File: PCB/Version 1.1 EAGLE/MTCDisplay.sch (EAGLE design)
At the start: 38 parts, among them IC1 74HC14N, J1 POWER_JACKPTH, U1 ATMEGA328P_PDIP, U2 57PC5FSWITCHCRAFT, U3 57PC5FSWITCHCRAFT, U4 57PC5FSWITCHCRAFT, U5 57PC5FSWITCHCRAFT, U6 MAX7219DIP, Y1 16MHz

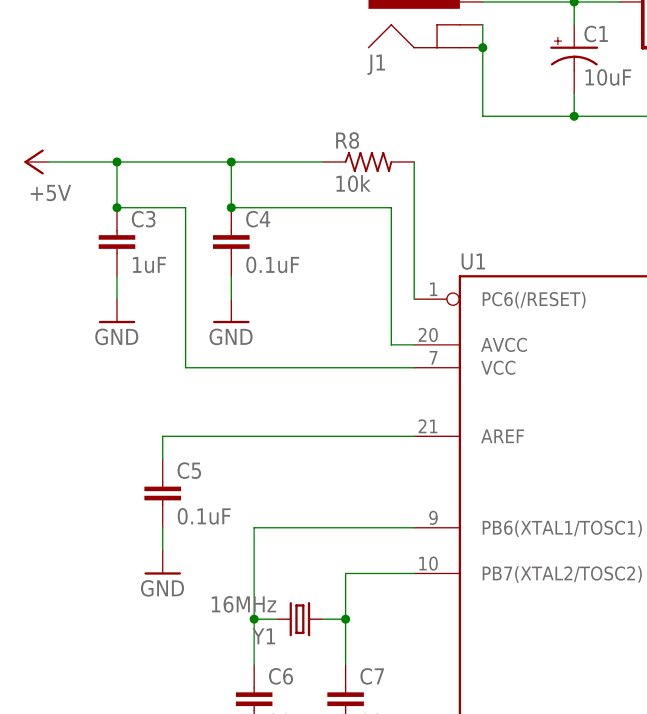
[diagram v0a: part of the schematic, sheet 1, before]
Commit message: update v1.1 schematics (replace 0.1uF cap package, add part names)
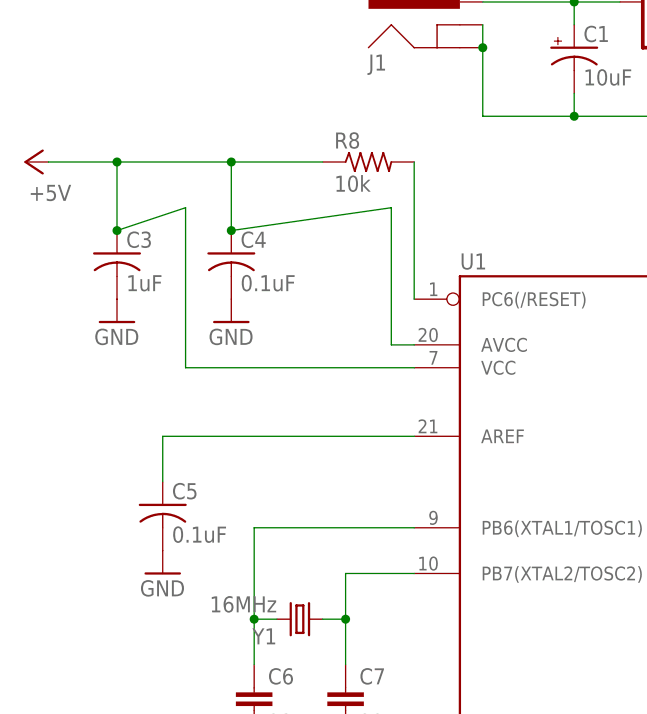
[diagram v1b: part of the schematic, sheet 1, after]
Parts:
- C10, C3, C4, C5, C8, C9: device SparkFun-Capacitors:0.1UF-50V-20%(PTH)KIT-EZ -> rcl:C-US025-025X050
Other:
- moved on the sheet: C10, C3, C4, C5, C8, C9

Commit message: Remove MIDI OUT, replace all TH capacitor with SMD
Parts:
- removed S1: RX-TX, SparkFun-Electromechanical:SWITCH-SPDTPTH
- C1, C11: value 10uF -> 10u; device resistor:CPOL-USE2-5 -> rcl:C-USC0805K
- C10, C4, C5, C8, C9: value 0.1uF -> 0.1u; device rcl:C-US025-025X050 -> rcl:C-USC0805K
- C2: value 22uF -> 22u; device resistor:CPOL-USE2-5 -> rcl:C-USC0805K
- C3: value 1uF -> 1u; device rcl:C-US025-025X050 -> rcl:C-USC0805K
- C6, C7: value 22pF -> 22p; device SparkFun-Capacitors:CAPPTH -> rcl:C-USC0805K
- D9: value (none) -> 1N4148
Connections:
- removed net RX/TX: IC1F.I, S1.P
- removed net UART-TX: S1.O, U1.PD1(TXD)
- net +5V: now also C11.1, C2.1; no longer C11.+, C2.+
- net GND: now also C1.2, C11.2, C2.2; no longer C1.-, C11.-, C2.-
- net N$16: now also C1.1; no longer C1.+
- net UART-RX: now also IC1F.I; no longer S1.S
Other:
- note added: "MIDI IN/THRU/OUT"
- moved on the sheet: C10, C3, C4, C5, C6, C7, C9, D9, IC1A, IC1B, IC1C, IC1D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
